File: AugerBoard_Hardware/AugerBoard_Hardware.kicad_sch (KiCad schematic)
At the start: 46 parts, among them J1 RJ45_LED_Shielded, J2 Conn_01x04_MountingPin, Q1 BSS138, Q2 BSS138, Q3 BSS138, SW1 SW_SPDT, SW2 SW_Push, SW3 SW_Push, SW4 SW_Push, U1 Teensy4.1_DEV-16771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

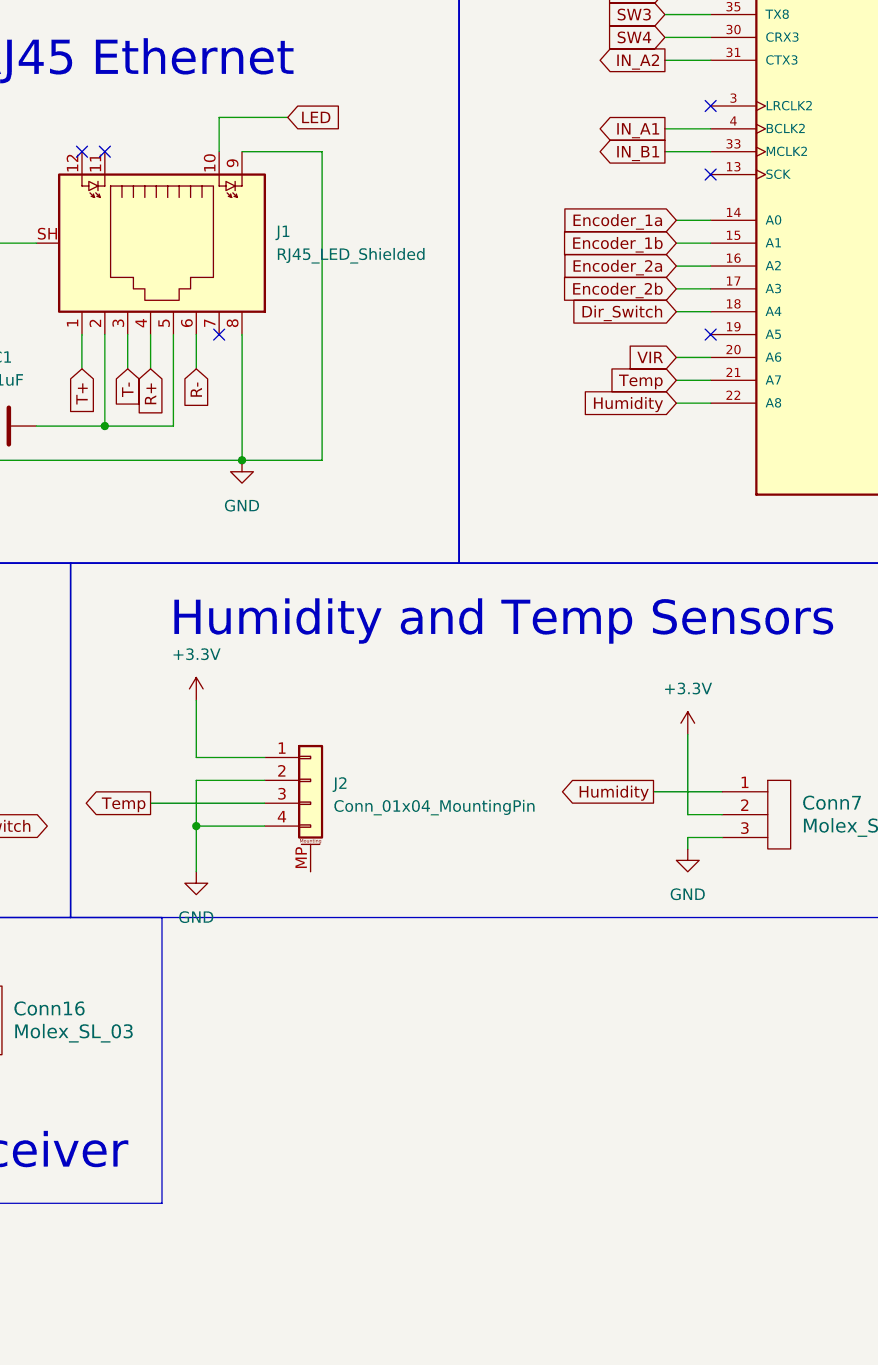
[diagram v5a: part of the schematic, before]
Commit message: UV Led connection added
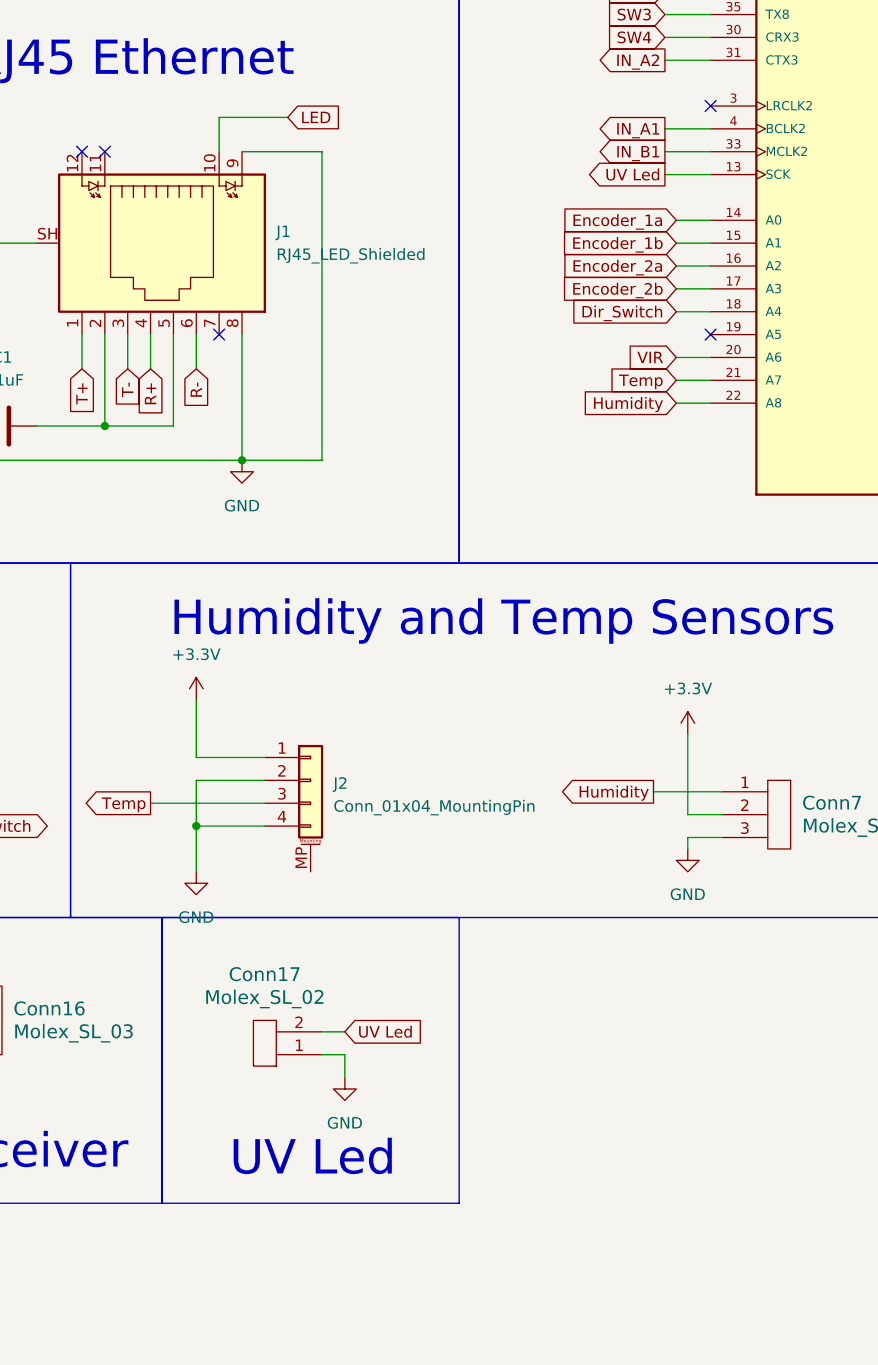
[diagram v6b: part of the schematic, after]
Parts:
- added Conn17: Molex_SL_02, MRDT_Connectors:MOLEX_SL_02_Vertical, symbol MRDT_Connectors:Molex_SL_02
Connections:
- net GND: now also Conn17.1
- net UV Led: now reaches U1.13 (SCK)
- net UV Led: now also Conn17.2
- no-connect marks 24 -> 23
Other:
- note added: "UV Led"
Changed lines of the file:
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@@
 	)
 	(no_connect
-		(at 224.79 92.71)
-	)
-	(no_connect
 		(at 157.48 90.17)
 	)
@@
 	(wire
 		(pts
+			(xy 181.61 187.96) (xy 184.15 187.96)
+		)
+		(stroke
+			(width 0)
+			(type default)
+		)
+	)
+	(wire
+		(pts
 			(xy 220.98 97.79) (xy 224.79 97.79)
 		)
@@
 	(wire
 		(pts
+			(xy 219.71 92.71) (xy 224.79 92.71)
+		)
+		(stroke
+			(width 0)
+			(type default)
+		)
+	)
+	(wire
+		(pts
 			(xy 336.55 113.03) (xy 344.17 113.03)
 		)
@@
 	(wire
 		(pts
+			(xy 181.61 190.5) (xy 184.15 190.5)
+		)
+		(stroke
+			(width 0)
+			(type default)
+		)
+	)
+	(wire
+		(pts
 			(xy 265.43 107.95) (xy 271.78 107.95)
 		)
@@
 	(wire
 		(pts
+			(xy 184.15 190.5) (xy 184.15 193.04)
+		)
+		(stroke
+			(width 0)
+			(type default)
+		)
+	)
+	(wire
+		(pts
 			(xy 307.34 90.17) (xy 316.23 90.17)
 		)
@@
 	)
 	(rectangle
+		(start 163.83 175.26)
+		(end 196.85 207.01)
+		(stroke
+			(width 0)
+			(type default)
+		)
+		(fill
+			(type none)
+		)
+	)
+	(rectangle
 		(start 153.67 135.89)
 		(end 250.19 175.26)
@@
 		)
 	)
+	(text "UV Led\n"
+		(exclude_from_sim no)
+		(at 180.594 202.184 0)
+		(effects
+			(font
+				(size 3.81 3.81)
+			)
+		)
+	)
 	(text "DumbMoCo Connections"
 		(exclude_from_sim no)
@@
 		)
 	)
+	(global_label "UV Led"
+		(shape output)
+		(at 219.71 92.71 180)
+		(fields_autoplaced yes)
+		(effects
+			(font
+				(size 1.27 1.27)
+			)
+			(justify right)
+		)
+		(property "Intersheetrefs" "${INTERSHEET_REFS}"
+			(at 210.0724 92.71 0)
+			(effects
+				(font
+					(size 1.27 1.27)
+				)
+				(justify right)
+				(hide yes)
+			)
+		)
+	)
 	(global_label "CS2"
 		(shape output)
@@
 		)
 	)
+	(global_label "UV Led"
+		(shape input)
+		(at 184.15 187.96 0)
+		(fields_autoplaced yes)
+		(effects
+			(font
+				(size 1.27 1.27)
+			)
+			(justify left)
+		)
+		(property "Intersheetrefs" "${INTERSHEET_REFS}"
+			(at 193.7876 187.96 0)
+			(effects
+				(font
+					(size 1.27 1.27)
+				)
+				(justify left)
+				(hide yes)
+			)
+		)
+	)
 	(global_label "LimitSwitch4"
 		(shape output)
@@
 	)
 	(symbol
+		(lib_id "power:GND")
+		(at 184.15 193.04 0)
+		(unit 1)
+		(exclude_from_sim no)
+		(in_bom yes)
+		(on_board yes)
+		(dnp no)
+		(fields_autoplaced yes)
+		(property "Reference" "#PWR027"
+			(at 184.15 199.39 0)
+			(effects
+				(font
+					(size 1.27 1.27)
+				)
+				(hide yes)
+			)
+		)
+		(property "Value" "GND"
+			(at 184.15 198.12 0)
+			(effects
+				(font
+					(size 1.27 1.27)
+				)
+			)
+		)
+		(property "Footprint" ""
+			(at 184.15 193.04 0)
+			(effects
+				(font
+					(size 1.27 1.27)
+				)
+				(hide yes)
+			)
+		)
+		(property "Datasheet" ""
+			(at 184.15 193.04 0)
+			(effects
+				(font
+					(size 1.27 1.27)
+				)
+				(hide yes)
+			)
+		)
+		(property "Description" "Power symbol creates a global label with name \"GND\" , ground"
+			(at 184.15 193.04 0)
+			(effects
+				(font
+					(size 1.27 1.27)
+				)
+				(hide yes)
+			)
+		)
+		(pin "1"
+		)
+		(instances
+			(project ""
+				(path "/eb675789-6cce-4465-8b28-94d3d6dee9aa"
+					(reference "#PWR027")
+					(unit 1)
+				)
+			)
+		)
+	)
+	(symbol
 		(lib_id "power:+3.3V")
 		(at 273.05 26.67 0)
@@
 					(unit 1)
 				)
+			)
+		)
+	)
+	(symbol
+		(lib_id "MRDT_Connectors:Molex_SL_02")
+		(at 176.53 186.69 180)
+		(unit 1)
+		(exclude_from_sim no)
+		(in_bom yes)
+		(on_board yes)
+		(dnp no)
+		(fields_autoplaced yes)
+		(property "Reference" "Conn17"
+			(at 175.26 181.61 0)
+			(effects
+				(font
+					(size 1.524 1.524)
+				)
+			)
+		)
+		(property "Value" "Molex_SL_02"
+			(at 175.26 184.15 0)
+			(effects
+				(font
+					(size 1.524 1.524)
+				)
+			)
+		)
+		(property "Footprint" "MRDT_Connectors:MOLEX_SL_02_Vertical"
+			(at 176.53 184.15 0)
+			(effects
+				(font
+					(size 1.524 1.524)
+				)
+				(hide yes)
+			)
+		)
+		(property "Datasheet" ""
+			(at 176.53 184.15 0)
+			(effects
+				(font
+					(size 1.524 1.524)
+				)
+				(hide yes)
+			)
+		)
+		(property "Description" ""
+			(at 176.53 186.69 0)
+			(effects
+				(font
+					(size 1.27 1.27)
+				)
+				(hide yes)
+			)
+		)
+		(pin "1"
+		)
+		(pin "2"
+		)
+		(instances
+			(project ""
+				(path "/eb675789-6cce-4465-8b28-94d3d6dee9aa"
+					(reference "Conn17")
+					(unit 1)
+				)

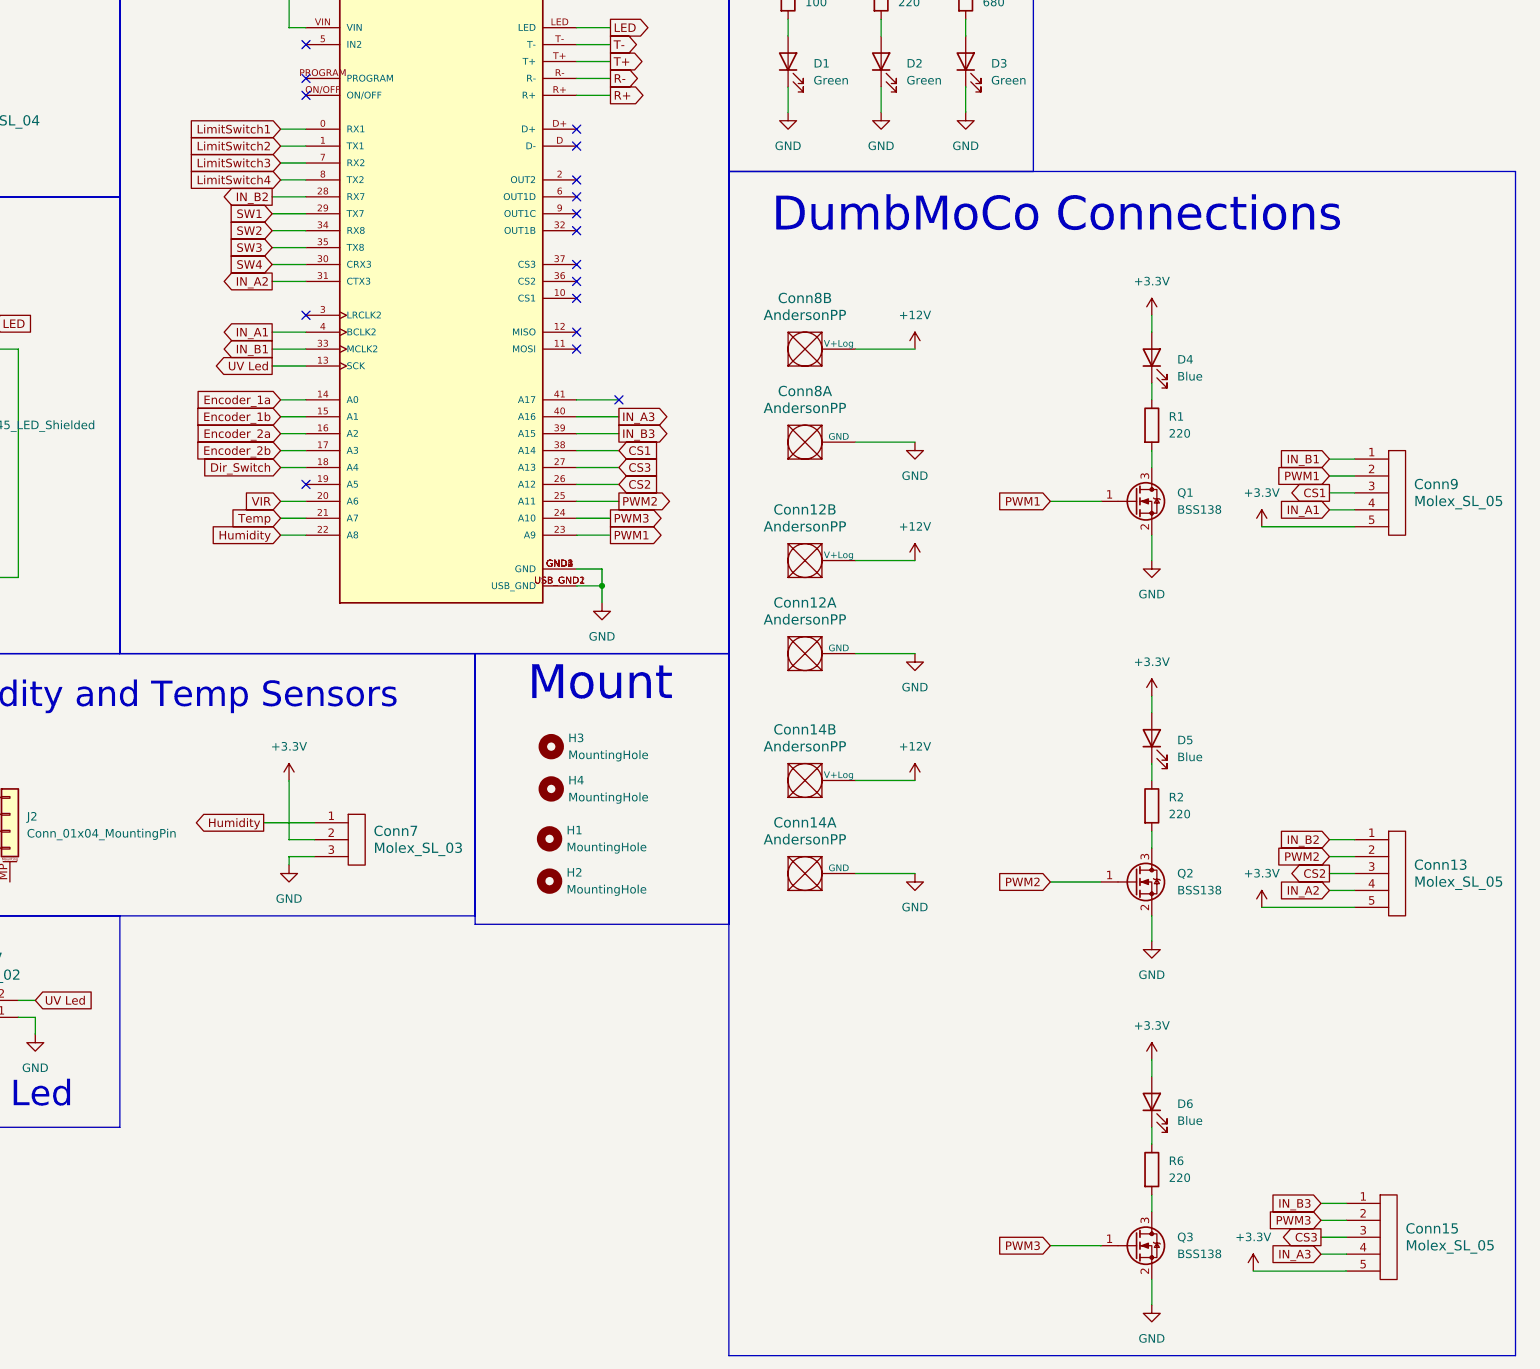
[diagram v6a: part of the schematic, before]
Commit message: vesc connections added, some traces rerouted, silkscreens added
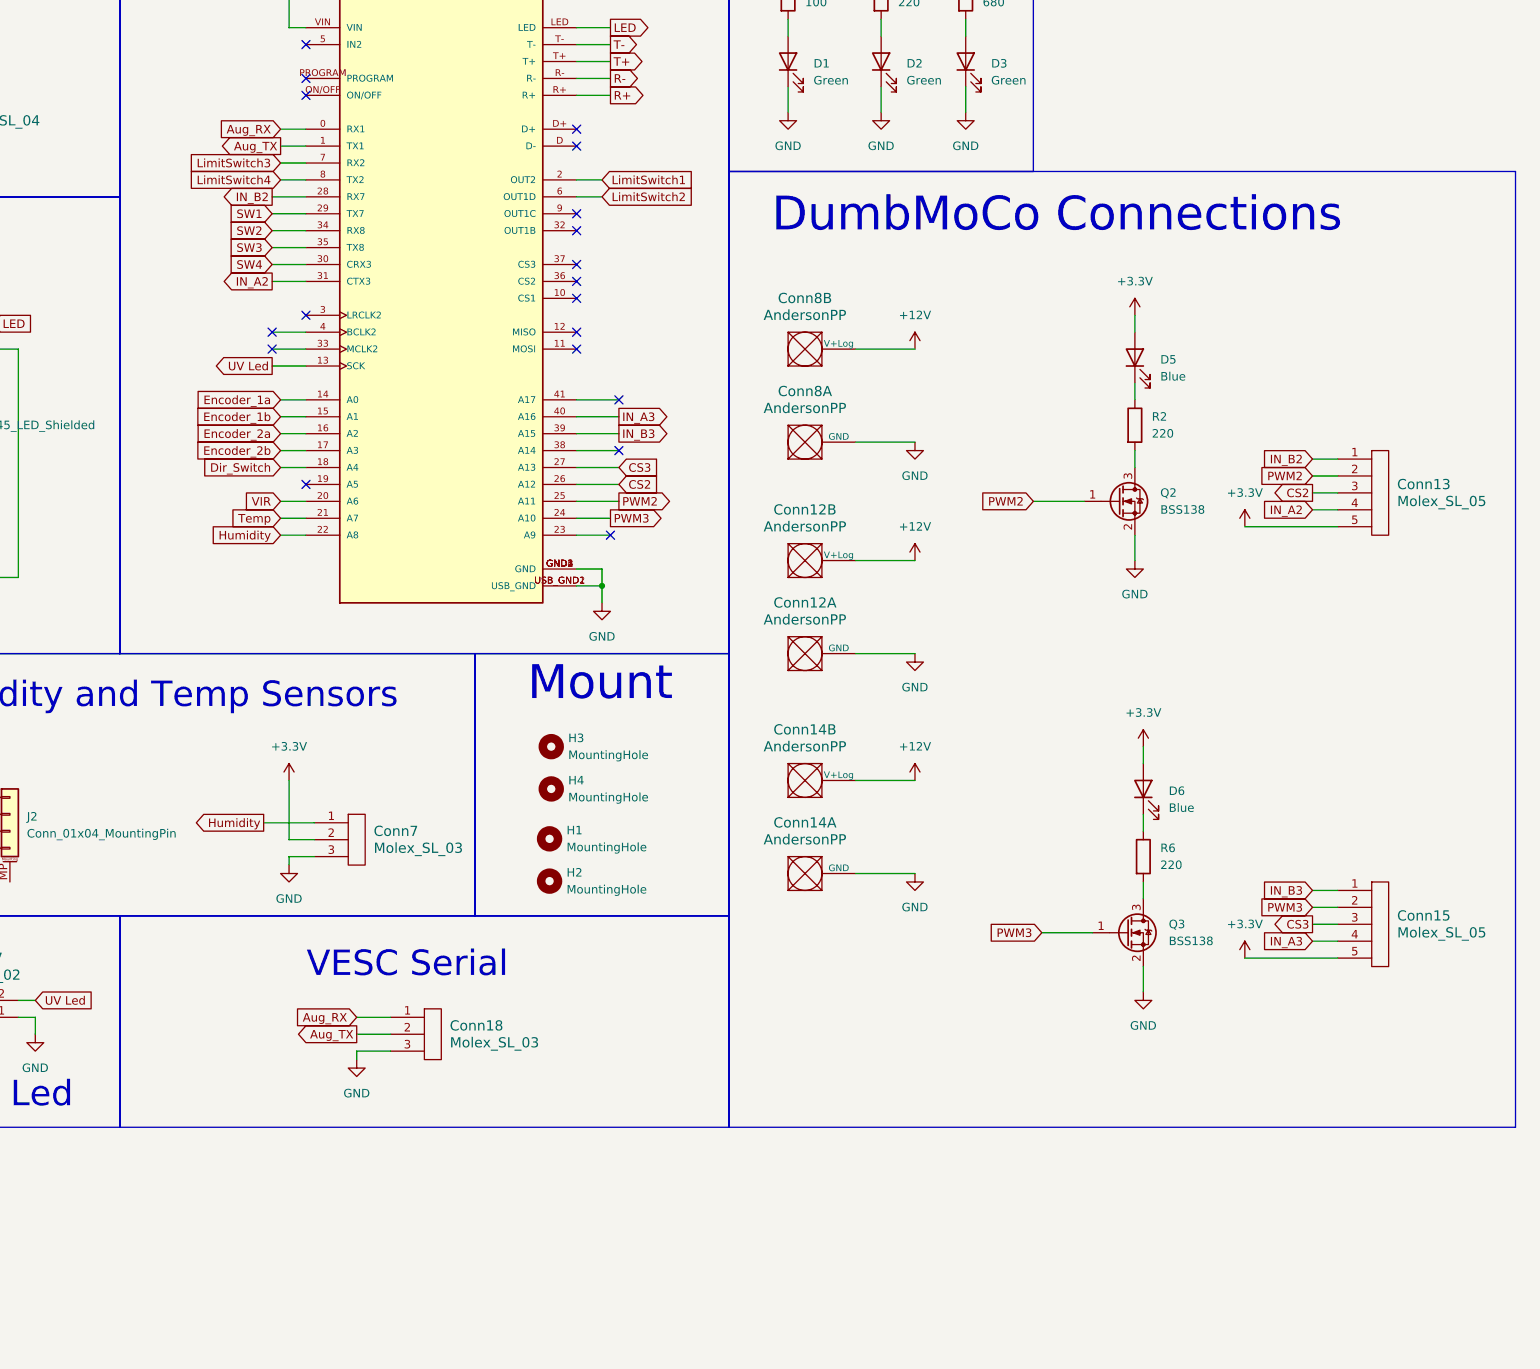
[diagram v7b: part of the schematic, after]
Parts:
- removed Conn9: Molex_SL_05, MRDT_Connectors:MOLEX_SL_05_Vertical, symbol MRDT_Connectors:Molex_SL_05
- removed D4: Blue, LED_SMD:LED_0603_1608Metric_Pad1.05x0.95mm_HandSolder, symbol Device:LED
- removed Q1: BSS138, Package_TO_SOT_SMD:SOT-23, symbol Transistor_FET:BSS138
- removed R1: 220, Resistor_SMD:R_0603_1608Metric_Pad0.98x0.95mm_HandSolder, symbol Device:R
- added Conn18: Molex_SL_03, MRDT_Connectors:MOLEX_SL_03_Vertical, symbol MRDT_Connectors:Molex_SL_03
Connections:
- net GND: now also Conn18.3
- net LimitSwitch1: now also U1.2 (OUT2); no longer U1.0 (RX1)
- net LimitSwitch2: now also U1.6 (OUT1D); no longer U1.1 (TX1)
- net CS1: no longer names the net of U1.38 (A14)
- net IN_A1: no longer names the net of U1.4 (BCLK2)
- net IN_B1: no longer names the net of U1.33 (MCLK2)
- net PWM1: no longer names the net of U1.23 (A9)
- new net Aug_RX: Conn18.1, U1.0 (RX1)
- new net Aug_TX: Conn18.2, U1.1 (TX1)
- no-connect marks 23 -> 25
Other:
- note added: "VESC Serial"
- moved on the sheet: Conn13, Conn15, D5, D6, Q2, Q3, R2, R6

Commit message: Schematic probably correct, layout fucked
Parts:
- removed Conn11: Molex_SL_02, MRDT_Connectors:MOLEX_SL_02_Vertical, symbol MRDT_Connectors:Molex_SL_02
- added Conn19, Conn9: Molex_SL_03, MRDT_Connectors:MOLEX_SL_03_Vertical, symbol MRDT_Connectors:Molex_SL_03
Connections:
- net +5V: now also Conn19.1, Conn9.1
- net GND: now also Conn19.3, Conn9.3
- net ServoPWM1: now reaches U1.23 (A9)
- net ServoPWM1: now also Conn9.2
- net ServoPWM2: now reaches U1.38 (A14)
- net ServoPWM2: now also Conn19.2
- no-connect marks 25 -> 23
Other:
- note added: "Servos"
- moved on the sheet: Conn17, Conn18
